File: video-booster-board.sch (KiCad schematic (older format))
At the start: 113 parts, among them J1 0473460001, J2 HDMI-PE10-19-LF, J3 HDMI-PE10-19-LF, J4 M20-9990246, J5 M20-9990246, J6 685119134923_, J7 M20-9990246, J8 M20-9990246, J9 685119134923_, U1 PTN3363, U3 PTN3363, U4 LP2985-33DBVR

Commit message: Power management options added
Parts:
- added C31, C33: C_100n_0402_6V3, antmicro-footprints:0402-cap, symbol video-booster-board-rescue:C_100n_0402_6V3-antmicroCapacitors0402
- added C34: C_1u_0402, antmicro-footprints:0402-cap, symbol video-booster-board-rescue:C_1u_0402-antmicroCapacitors0402
- added C36: C_4u7_0603, antmicro-footprints:0603-cap, symbol video-booster-board-rescue:C_4u7_0603-antmicroCapacitors0603
- added D1, D4, D5, D6, D7: BAT54-02V-V-G, antmicro-footprints:SOD-523, symbol video-booster-board-rescue:BAT54-02V-V-G-antmicroDiodesRectifiersSingle
- added J10: 640456-2, antmicro-footprints:PinHeader_1x2_P2.54mm_Drill1.02mm, symbol antmicroRectangularConnectorsHeadersMalePins:640456-2
- added R30: R_806k_0402, antmicro-footprints:0402-res, symbol antmicroResistors0402:R_806k_0402
- added R56, R57: R_1R_0402, antmicro-footprints:0402-res, symbol antmicroResistors0402:R_1R_0402
- added R60, R62, R64, R68: R_27k_0402, antmicro-footprints:0402-res, symbol antmicroResistors0402:R_27k_0402
- added R61, R63, R65, R69: R_4k7_0402, antmicro-footprints:0402-res, symbol antmicroResistors0402:R_4k7_0402
- added U2: TPS2110APW, antmicro-footprints:TSSOP-8_W4.4mm, symbol antmicroPMICPowerDistributionSwitchesLoadDrivers:TPS2110APW
- gave numbers to parts that had none: 21
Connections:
- net labels added: +5VA, RX_SINK_5V, RX_SRC_5V, TX_SINK_5V, TX_SINK_PWR, TX_SRC_5V
- wire segments 494 -> 546
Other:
- note added: "+5V Auxillary"
- note removed: "changes..."
- moved on the sheet: C1, C26, C27, C28, C29, C30, C37, C5, C6, D2, D3, D8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

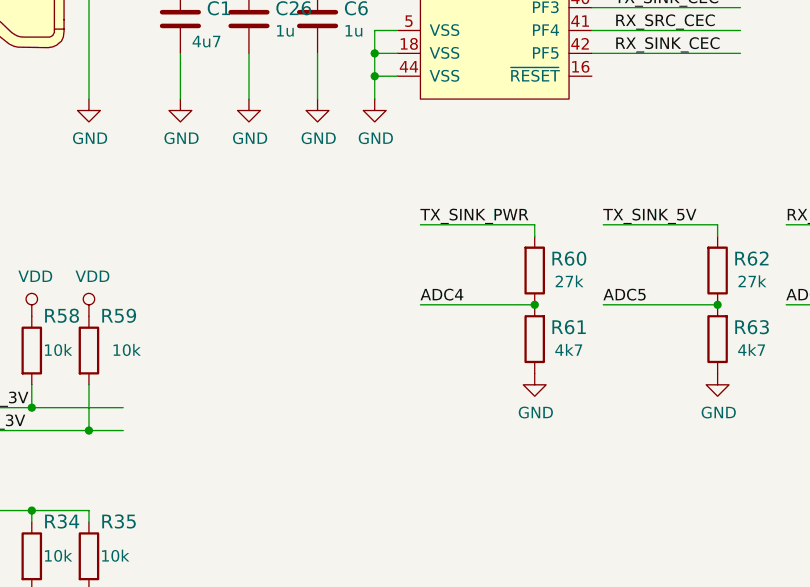
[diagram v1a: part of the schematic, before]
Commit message: Current sensing opamp added
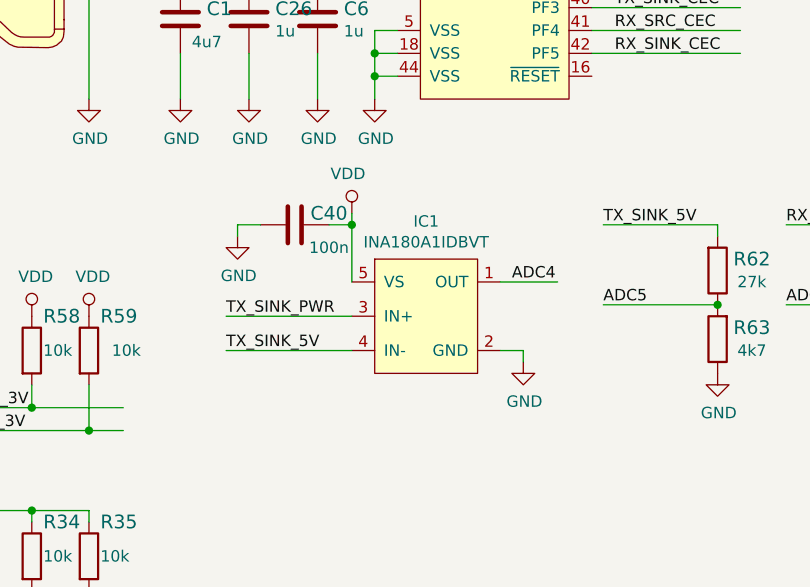
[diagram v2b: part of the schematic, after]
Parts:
- removed R60: R_27k_0402, antmicro-footprints:0402-res, symbol antmicroResistors0402:R_27k_0402
- removed R61: R_4k7_0402, antmicro-footprints:0402-res, symbol antmicroResistors0402:R_4k7_0402
- added C40: C_100n_0402_6V3, antmicro-footprints:0402-cap, symbol video-booster-board-rescue:C_100n_0402_6V3-antmicroCapacitors0402
- added IC1: INA180A1IDBVT, antmicro-footprints:SOT-23-5, symbol antmicroOperationalAmplifiers:INA180A1IDBVT
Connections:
- wire segments 546 -> 553
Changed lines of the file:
@@
 Text Label 8000 1650 0    50   ~ 0
 TX_SINK_PWR
-$Comp
-L antmicroResistors0402:R_4k7_0402 R61
-U 1 1 643030DE
-P 13050 9550
-F 0 "R61" V 13100 9400 60  0000 C CNN
-F 1 "R_4k7_0402" H 13050 9400 60  0001 C CNN
-F 2 "antmicro-footprints:0402-res" H 13250 9750 60  0001 L CNN
-F 3 "" H 13050 9550 50  0001 C CNN
-F 4 "PANASONIC_ELECTRONIC_COMPONENTS" H 13250 9950 60  0001 L CNN "Manufacturer"
-F 5 "ERJ2GEJ472X" H 13250 9850 60  0001 L CNN "MPN"
-F 6 "4k7" V 13000 9400 50  0000 C CNN "Val"
-	1    13050 9550
-	0    -1   -1   0
-$EndComp
-$Comp
-L antmicroResistors0402:R_27k_0402 R60
-U 1 1 64303E80
-P 13050 9250
-F 0 "R60" V 13100 9400 60  0000 C CNN
-F 1 "R_27k_0402" H 13050 9100 60  0001 C CNN
-F 2 "antmicro-footprints:0402-res" H 13250 9450 60  0001 L CNN
-F 3 "" H 13050 9250 50  0001 C CNN
-F 4 "PANASONIC_ELECTRONIC_COMPONENTS" H 13250 9650 60  0001 L CNN "Manufacturer"
-F 5 "ERJ2RKF2702X" H 13250 9550 60  0001 L CNN "MPN"
-F 6 "27k" V 13000 9400 50  0000 C CNN "Val"
-	1    13050 9250
-	0    1    -1   0
-$EndComp
-$Comp
-L power:GND #PWR074
-U 1 1 6436DAF2
-P 13050 9700
-F 0 "#PWR074" H 13050 9450 50  0001 C CNN
-F 1 "GND" H 13055 9527 50  0000 C CNN
-F 2 "" H 13050 9700 50  0001 C CNN
-F 3 "" H 13050 9700 50  0001 C CNN
-	1    13050 9700
-	1    0    0    -1
-$EndComp
-Connection ~ 13050 9400
-Wire Wire Line
-	13050 9100 13050 9050
-Text Label 12550 9400 0    50   ~ 0
+Text Label 12950 9300 0    50   ~ 0
 ADC4
 Text Label 13350 9400 0    50   ~ 0
@@
 	1    0    0    -1
 $EndComp
-Text Label 13350 9050 0    50   ~ 0
+Text Label 11700 9600 0    50   ~ 0
 TX_SINK_5V
-Text Label 12550 9050 0    50   ~ 0
+Text Label 11700 9450 0    50   ~ 0
 TX_SINK_PWR
 $Comp
@@
 Text Label 14150 9050 0    50   ~ 0
 RX_SRC_5V
-Wire Wire Line
-	13050 9400 12550 9400
-Wire Wire Line
-	13050 9050 12550 9050
 $Comp
 L antmicroResistors0402:R_4k7_0402 R63
@@
 	1    0    0    -1
 $EndComp
+$Comp
+L antmicroOperationalAmplifiers:INA180A1IDBVT IC1
+U 1 1 5DD3122C
+P 12350 9700
+F 0 "IC1" H 12575 10365 50  0000 C CNN
+F 1 "INA180A1IDBVT" H 12575 10274 50  0000 C CNN
+F 2 "antmicro-footprints:SOT-23-5" H 12400 10250 50  0001 C CNN
+F 3 "http://www.ti.com/lit/ds/symlink/ina180.pdf" H 12400 10250 50  0001 C CNN
+	1    12350 9700
+	1    0    0    -1
+$EndComp
+$Comp
+L video-booster-board-rescue:C_100n_0402_6V3-antmicroCapacitors0402 C40
+U 1 1 5DDC8A4E
+P 12000 9050
+F 0 "C40" V 11950 9200 60  0000 C CNN
+F 1 "C_100n_0402_6V3" H 12000 8900 60  0001 C CNN
+F 2 "antmicro-footprints:0402-cap" H 12200 9250 60  0001 L CNN
+F 3 "" H 12000 9050 50  0001 C CNN
+F 4 "Walsin" H 12200 9450 60  0001 L CNN "Manufacturer"
+F 5 "0402X104K6R3CT" H 12200 9350 60  0001 L CNN "MPN"
+F 6 "100n" V 12100 9200 50  0000 C CNN "Val"
+	1    12000 9050
+	0    1    1    0
+$EndComp
+$Comp
+L power:VDD #PWR087
+U 1 1 5DDCADC8
+P 12250 9000
+F 0 "#PWR087" H 12250 8850 50  0001 C CNN
+F 1 "VDD" H 12267 9173 50  0000 C CNN
+F 2 "" H 12250 9000 50  0001 C CNN
+F 3 "" H 12250 9000 50  0001 C CNN
+	1    12250 9000
+	-1   0    0    -1
+$EndComp
+$Comp
+L power:GND #PWR074
+U 1 1 5DDD8114
+P 11750 9100
+F 0 "#PWR074" H 11750 8850 50  0001 C CNN
+F 1 "GND" H 11755 8927 50  0000 C CNN
+F 2 "" H 11750 9100 50  0001 C CNN
+F 3 "" H 11750 9100 50  0001 C CNN
+	1    11750 9100
+	1    0    0    -1
+$EndComp
+Wire Wire Line
+	12150 9050 12250 9050
+Wire Wire Line
+	11850 9050 11750 9050
+Wire Wire Line
+	12250 9450 11700 9450
+Wire Wire Line
+	11700 9600 12250 9600
+Wire Wire Line
+	12900 9300 13150 9300
+$Comp
+L power:GND #PWR088
+U 1 1 5E0280DA
+P 13000 9650
+F 0 "#PWR088" H 13000 9400 50  0001 C CNN
+F 1 "GND" H 13005 9477 50  0000 C CNN
+F 2 "" H 13000 9650 50  0001 C CNN
+F 3 "" H 13000 9650 50  0001 C CNN
+	1    13000 9650
+	1    0    0    -1
+$EndComp
+Wire Wire Line
+	13000 9650 13000 9600
+Wire Wire Line
+	13000 9600 12900 9600
+Wire Wire Line
+	12250 9050 12250 9300
+Wire Wire Line
+	12250 9000 12250 9050
+Connection ~ 12250 9050
+Wire Wire Line
+	11750 9100 11750 9050
+Text Label 13350 9050 0    50   ~ 0
+TX_SINK_5V
 $EndSCHEMATC

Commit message: Pinout adjustments. Placement of new components
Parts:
- removed D1, D2, D3, D4, D5, D6: BAT54-02V-V-G, antmicro-footprints:SOD-523, symbol video-booster-board-rescue:BAT54-02V-V-G-antmicroDiodesRectifiersSingle
- removed J10: 640456-2, antmicro-footprints:PinHeader_1x2_P2.54mm_Drill1.02mm, symbol antmicroRectangularConnectorsHeadersMalePins:640456-2
- removed J4, J5, J7, J8: M20-9990246, antmicro-footprints:PinHeader_1x2_P2.54mm, symbol video-booster-board-rescue:M20-9990246-antmicroRectangularConnectorsHeadersMale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
- added D1, D2, D3, D4, D5, D6: BAT54-02V-V-G, antmicro-footprints:SOD-523, symbol antmicroDiodesRectifiersSingle:BAT54-02V-V-G
- added J10: M20-9990246, antmicro-footprints:PinHeader_1x2_P2.54mm, symbol antmicroRectangularConnectorsHeadersMalePins:M20-9990246
- added SW1: 1571983-5, antmicro-footprints:1571983-5, symbol antmicroSlideSwitches:1571983-5
- D7: symbol video-booster-board-rescue:BAT54-02V-V-G-antmicroDiodesRectifiersSingle -> antmicroDiodesRectifiersSingle:BAT54-02V-V-G
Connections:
- net labels removed: RX_5V, TX_5V
- wire segments 553 -> 559
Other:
- moved on the sheet: R14, R15, R39, R40

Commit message: Schematic sheet changed to A2, added schematic sections
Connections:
- wire segments 559 -> 546
- no-connect marks 0 -> 2
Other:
- note added: "Beamer"
- note added: "Config"
- note added: "HDMI receiver"
- note added: "HDMI transmitter"
- note added: "MCU"
- note added: "Opsis (RX)"
- note added: "Opsis (TX)"
- note added: "Power supply"
- note added: "Presenter"
- moved on the sheet: C1, C10, C11, C12, C13, C14, C15, C16, C17, C18, C19, C2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

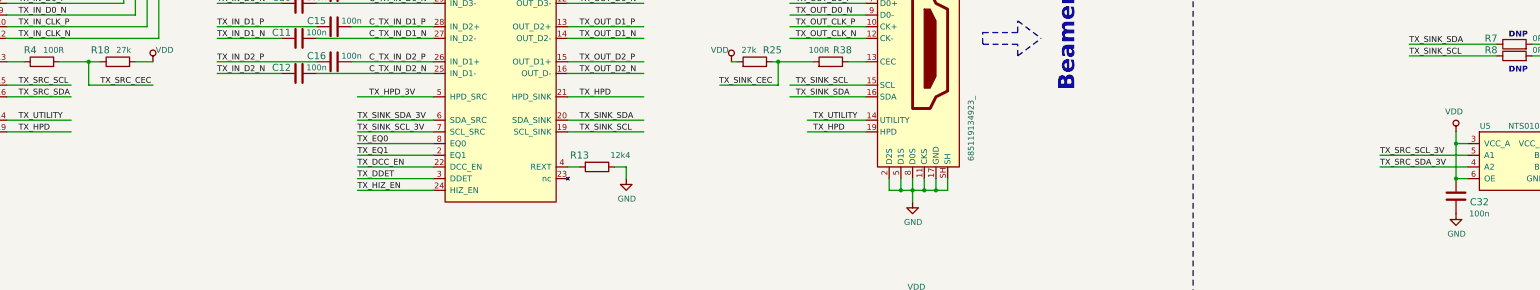
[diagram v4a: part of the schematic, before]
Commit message: Added notes to HDMI/EDID
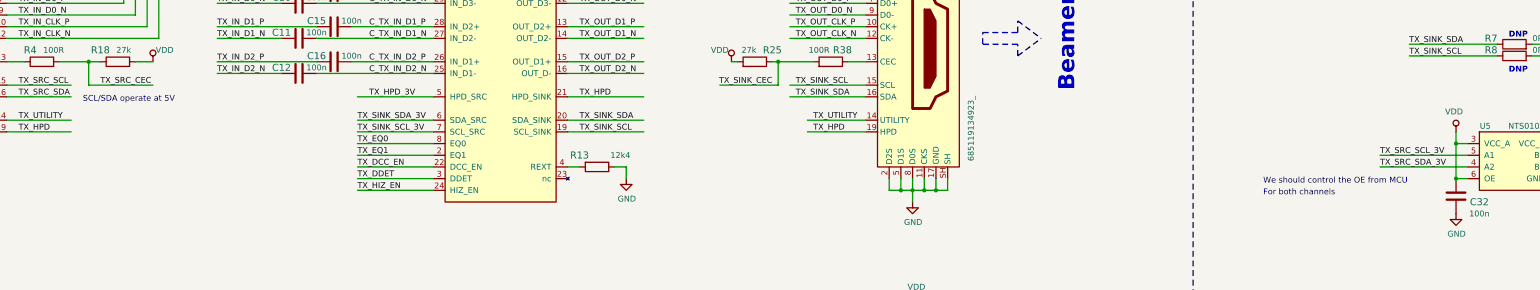
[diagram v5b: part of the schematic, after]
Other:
- note added: "For both channels"
- note added: "SCL/SDA operate at 5V"
- note added: "We should control the OE from MCU"
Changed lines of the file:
@@
 Text Notes 13150 8050 0    138  ~ 28
 MCU
+Text Notes 3250 3700 0    50   ~ 0
+SCL/SDA operate at 5V
+Text Notes 13350 4400 0    50   ~ 0
+We should control the OE from MCU
+Text Notes 13350 4500 0    50   ~ 0
+For both channels
 $EndSCHEMATC

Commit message: VDD replaced with +3V3
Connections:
- net labels added: +3V3
- net labels removed: VDD
- wire segments 546 -> 548
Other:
- note removed: "For both channels"
- note removed: "We should control the OE from MCU"

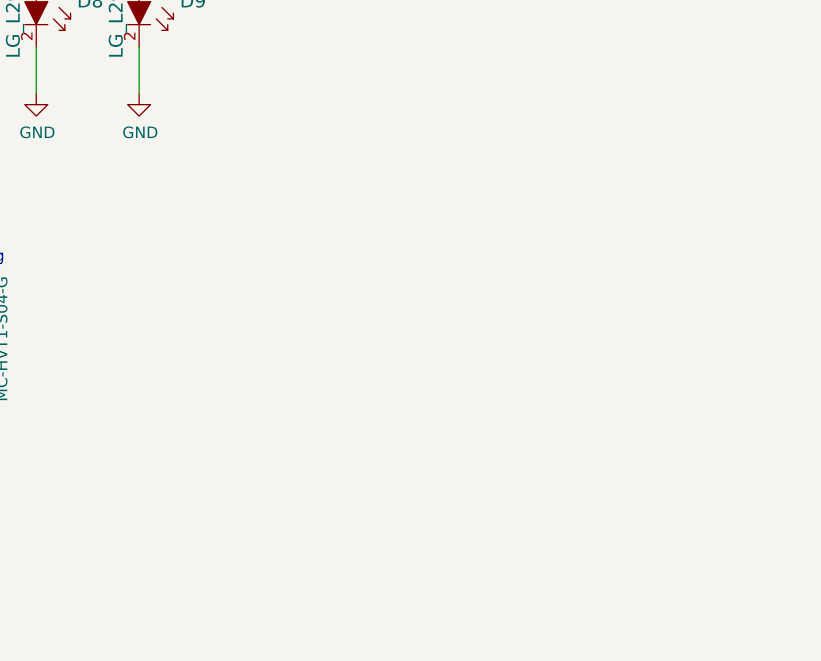
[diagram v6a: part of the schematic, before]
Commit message: CEC clamp diodes added. Open hardware logo added
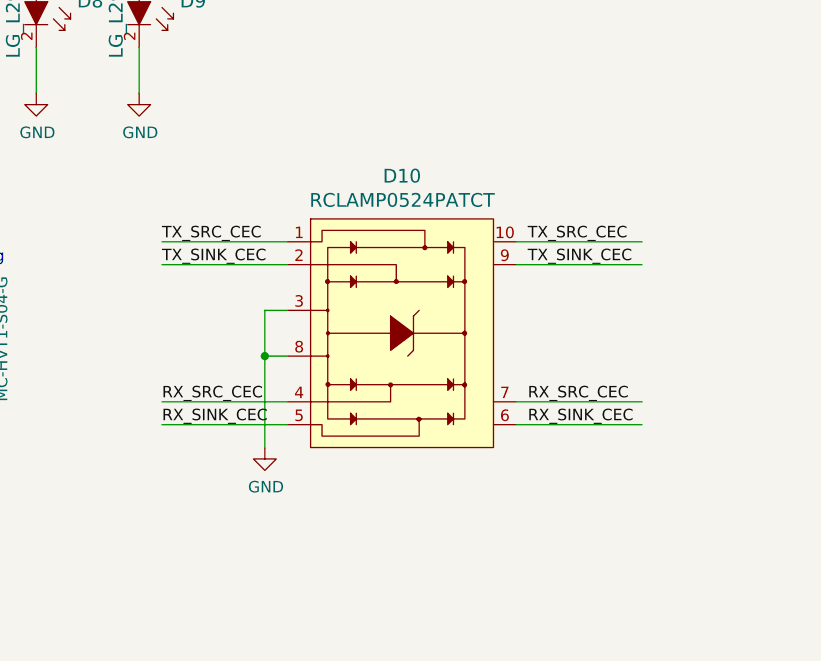
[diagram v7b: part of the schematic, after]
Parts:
- added D10: RCLAMP0524PATCT, antmicro-footprints:UFDFN-10_2.5x1mm, symbol antmicroTVSDiodes:RCLAMP0524PATCT
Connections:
- wire segments 548 -> 560

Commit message: Local libraries generated. SCH and PCB relinked to local libraries
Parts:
- C1, C36: footprint antmicro-footprints:0603-cap -> video-booster-board-footprints:0603-cap; symbol video-booster-board-rescue:C_4u7_0603-antmicroCapacitors0603 -> video-booster-board:C_4u7_0603-antmicroCapacitors0603
- C10, C11, C12, C13, C14, C15, C16, C18, C19, C2, C20, C21, C22, C23, C24, C25, C27, C3, C31, C32, C33, C35, C38, C39, C40, C7, C8, C9: footprint antmicro-footprints:0402-cap -> video-booster-board-footprints:0402-cap; symbol video-booster-board-rescue:C_100n_0402_6V3-antmicroCapacitors0402 -> video-booster-board:C_100n_0402_6V3-antmicroCapacitors0402
- C17, C4: footprint antmicro-footprints:0603-cap -> video-booster-board-footprints:0603-cap; symbol video-booster-board-rescue:C_10u_0603-antmicroCapacitors0603 -> video-booster-board:C_10u_0603-antmicroCapacitors0603
- C26, C34, C37, C5, C6: footprint antmicro-footprints:0402-cap -> video-booster-board-footprints:0402-cap; symbol video-booster-board-rescue:C_1u_0402-antmicroCapacitors0402 -> video-booster-board:C_1u_0402-antmicroCapacitors0402
- C28, C30: footprint antmicro-footprints:0402-cap -> video-booster-board-footprints:0402-cap; symbol video-booster-board-rescue:C_2u2_0402-antmicroCapacitors0402 -> video-booster-board:C_2u2_0402-antmicroCapacitors0402
- C29: footprint antmicro-footprints:0402-cap -> video-booster-board-footprints:0402-cap; symbol video-booster-board-rescue:C_10n_0402-antmicroCapacitors0402 -> video-booster-board:C_10n_0402-antmicroCapacitors0402
- D1, D2, D3, D4, D5, D6, D7: footprint antmicro-footprints:SOD-523 -> video-booster-board-footprints:SOD-523; symbol antmicroDiodesRectifiersSingle:BAT54-02V-V-G -> video-booster-board:BAT54-02V-V-G
- D10: footprint antmicro-footprints:UFDFN-10_2.5x1mm -> video-booster-board-footprints:UFDFN-10_2.5x1mm; symbol antmicroTVSDiodes:RCLAMP0524PATCT -> video-booster-board:RCLAMP0524PATCT
- D8, D9: footprint antmicro-footprints:LED_0603 -> video-booster-board-footprints:LED_0603; symbol antmicroLEDIndicationDiscrete:LG_L29K-G2J1-24-Z -> video-booster-board:LG_L29K-G2J1-24-Z
- IC1: footprint antmicro-footprints:SOT-23-5 -> video-booster-board-footprints:SOT-23-5; symbol antmicroOperationalAmplifiers:INA180A1IDBVT -> video-booster-board:INA180A1IDBVT
- J1: footprint antmicro-footprints:USB_Micro_B_Female_0473460001 -> video-booster-board-footprints:USB_Micro_B_Female_0473460001; symbol video-booster-board-rescue:0473460001-antmicroUSBDVIHDMIConnectors -> video-booster-board:0473460001-antmicroUSBDVIHDMIConnectors
- J10: footprint antmicro-footprints:PinHeader_1x2_P2.54mm -> video-booster-board-footprints:PinHeader_1x2_P2.54mm; symbol antmicroRectangularConnectorsHeadersMalePins:M20-9990246 -> video-booster-board:M20-9990246
- J11: footprint antmicro-footprints:PinHeader_1x4_P1.27mm_Drill.7mm -> video-booster-board-footprints:PinHeader_1x4_P1.27mm_Drill.7mm; symbol video-booster-board-rescue:MC-HVT1-S04-G-antmicroRectangularConnectorsHeadersMalePins -> video-booster-board:MC-HVT1-S04-G-antmicroRectangularConnectorsHeadersMalePins
- J2, J3: footprint antmicro-footprints:HDMI-PE10-19-LF -> video-booster-board-footprints:HDMI-PE10-19-LF; symbol video-booster-board-rescue:HDMI-PE10-19-LF-antmicroUSBDVIHDMIConnectors -> video-booster-board:HDMI-PE10-19-LF-antmicroUSBDVIHDMIConnectors
- J6, J9: footprint antmicro-footprints:HDMI_A_Female_685119134923 -> video-booster-board-footprints:HDMI_A_Female_685119134923; symbol video-booster-board-rescue:685119134923_-antmicroUSBDVIHDMIConnectors -> video-booster-board:685119134923_-antmicroUSBDVIHDMIConnectors
- R1, R2: footprint antmicro-footprints:0402-res -> video-booster-board-footprints:0402-res; symbol video-booster-board-rescue:R_15R_0402-antmicroResistors0402 -> video-booster-board:R_15R_0402-antmicroResistors0402
- R10, R21, R22, R23, R26, R28, R29, R31, R32, R34, R35, R36, R37, R39, R40, R58, R59, R9: footprint antmicro-footprints:0402-res -> video-booster-board-footprints:0402-res; symbol video-booster-board-rescue:R_10k_0402-antmicroResistors0402 -> video-booster-board:R_10k_0402-antmicroResistors0402
- R11, R12, R7, R8: footprint antmicro-footprints:0402-res -> video-booster-board-footprints:0402-res; symbol video-booster-board-rescue:R_0R_0402-antmicroResistors0402 -> video-booster-board:R_0R_0402-antmicroResistors0402
- R13, R17: footprint antmicro-footprints:0402-res -> video-booster-board-footprints:0402-res; symbol video-booster-board-rescue:R_12k4_0402-antmicroResistors0402 -> video-booster-board:R_12k4_0402-antmicroResistors0402
- R14, R15, R19, R24, R5, R6: footprint antmicro-footprints:0402-res -> video-booster-board-footprints:0402-res; symbol video-booster-board-rescue:R_100k_0402-antmicroResistors0402 -> video-booster-board:R_100k_0402-antmicroResistors0402
- R16, R38, R4, R41: footprint antmicro-footprints:0402-res -> video-booster-board-footprints:0402-res; symbol antmicroResistors0402:R_100R_0402 -> video-booster-board:R_100R_0402
- R18, R20, R25, R27, R62, R64, R68: footprint antmicro-footprints:0402-res -> video-booster-board-footprints:0402-res; symbol antmicroResistors0402:R_27k_0402 -> video-booster-board:R_27k_0402
- R3, R33, R42, R43, R44, R45, R46, R47, R48, R49, R50, R51, R52, R53, R54, R55: footprint antmicro-footprints:0402-res -> video-booster-board-footprints:0402-res; symbol video-booster-board-rescue:R_49R9_0402-antmicroResistors0402 -> video-booster-board:R_49R9_0402-antmicroResistors0402
- R30: footprint antmicro-footprints:0402-res -> video-booster-board-footprints:0402-res; symbol antmicroResistors0402:R_806k_0402 -> video-booster-board:R_806k_0402
- R56, R57: footprint antmicro-footprints:0402-res -> video-booster-board-footprints:0402-res; symbol antmicroResistors0402:R_1R_0402 -> video-booster-board:R_1R_0402
- R63, R65, R69: footprint antmicro-footprints:0402-res -> video-booster-board-footprints:0402-res; symbol antmicroResistors0402:R_4k7_0402 -> video-booster-board:R_4k7_0402
- R66, R67: footprint antmicro-footprints:0402-res -> video-booster-board-footprints:0402-res; symbol antmicroResistors0402:R_330R_0402 -> video-booster-board:R_330R_0402
- SW1: footprint antmicro-footprints:1571983-5 -> video-booster-board-footprints:1571983-5; symbol antmicroSlideSwitches:1571983-5 -> video-booster-board:1571983-5
- U1, U3: footprint antmicro-footprints:QFN-32-1EP_5x5mm -> video-booster-board-footprints:QFN-32-1EP_5x5mm; symbol video-booster-board-rescue:PTN3363-antmicroInterfaceDriversReceiversTransceivers -> video-booster-board:PTN3363-antmicroInterfaceDriversReceiversTransceivers
- U2: footprint antmicro-footprints:TSSOP-8_W4.4mm -> video-booster-board-footprints:TSSOP-8_W4.4mm; symbol antmicroPMICPowerDistributionSwitchesLoadDrivers:TPS2110APW -> video-booster-board:TPS2110APW
- U4: footprint antmicro-footprints:SOT-753 -> video-booster-board-footprints:SOT-753; symbol video-booster-board-rescue:LP2985-33DBVR-antmicroPMICVoltageRegulatorsLinear -> video-booster-board:LP2985-33DBVR-antmicroPMICVoltageRegulatorsLinear
- U5, U7: footprint antmicro-footprints:PSON50P100X195X50-8N -> video-booster-board-footprints:PSON50P100X195X50-8N; symbol antmicroLogicTranslatorsLevelShifters:NTS0102GT -> video-booster-board:NTS0102GT
- U6: footprint antmicro-footprints:TQFP-48_7x7mm -> video-booster-board-footprints:TQFP-48_7x7mm; symbol video-booster-board-rescue:EFM32HG321-antmicroMicrocontrollers -> video-booster-board:EFM32HG321-antmicroMicrocontrollers
